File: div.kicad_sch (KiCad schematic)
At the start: 6 parts, among them X1 DF40HC_3.0_-100DS-0.4V_58, X2 DF40HC_3.0_-100DS-0.4V_58

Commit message: partnumber, manufaturerer and description cleanup completed
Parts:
- MP1, MP2, MP3, MP4: Description_1 steel, tin plated with internal thread M2.5 non stop outer 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 -> (none); MF Wurth Electronics -> (none); MP 9774030151R -> (none); MPN (none) -> 9774030151R; Manufacturer (none) -> Wurth Electronics
- X1, X2: Description_1 100 Position Connector Receptacle, Center Strip Contacts Su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 -> (none); MANUFACTURER HRS -> (none); MP DF40HC(3.0)-100DS-0.4V(58 -> (none); MPN (none) -> DF40HC(3.0)-100DS-0.4V(58; Manufacturer (none) -> HRS

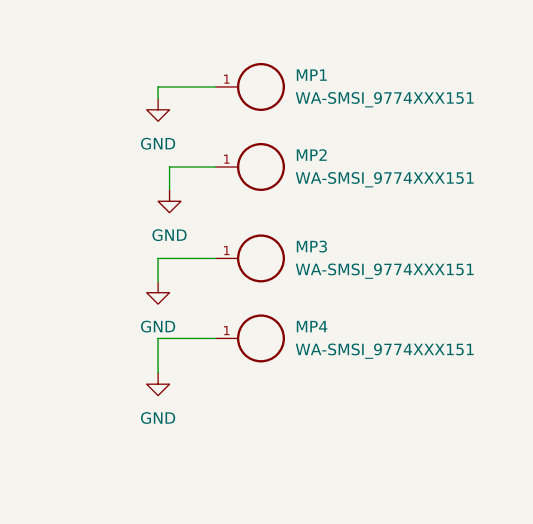
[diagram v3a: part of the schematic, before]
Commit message: update licence to CERN-OHL-S
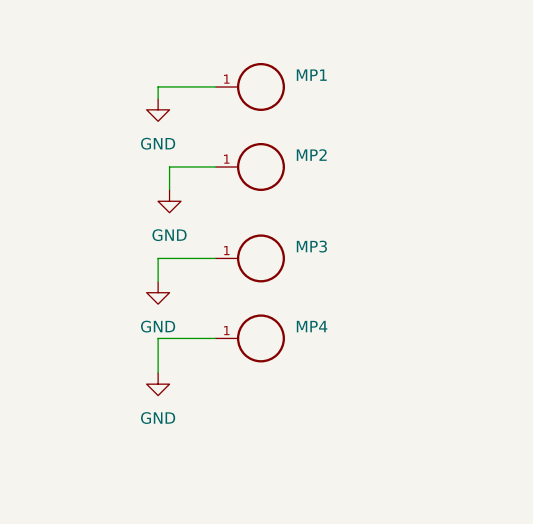
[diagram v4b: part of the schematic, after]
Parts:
- MP1, MP2, MP3, MP4: value WA-SMSI_9774XXX151 -> M2.5 x 3mm; VALUE M2.5 x 3mm -> (none)
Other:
- company: (none) -> NTNU, NINA
- title: (none) -> Audiograb
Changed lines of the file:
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@@
 (kicad_sch
-	(version 20250114)
+	(version 20260306)
 	(generator "eeschema")
-	(generator_version "9.0")
+	(generator_version "10.0")
 	(paper "A4")
+	(title_block
+		(title "Audiograb")
+		(date "2026-02-13")
+		(rev "0")
+		(company "NTNU, NINA")
+		(comment 1 "https://github.com/oveljosland/audiograb-pcb/")
+		(comment 2 "Licenced under CERN-OHL-S")
+	)

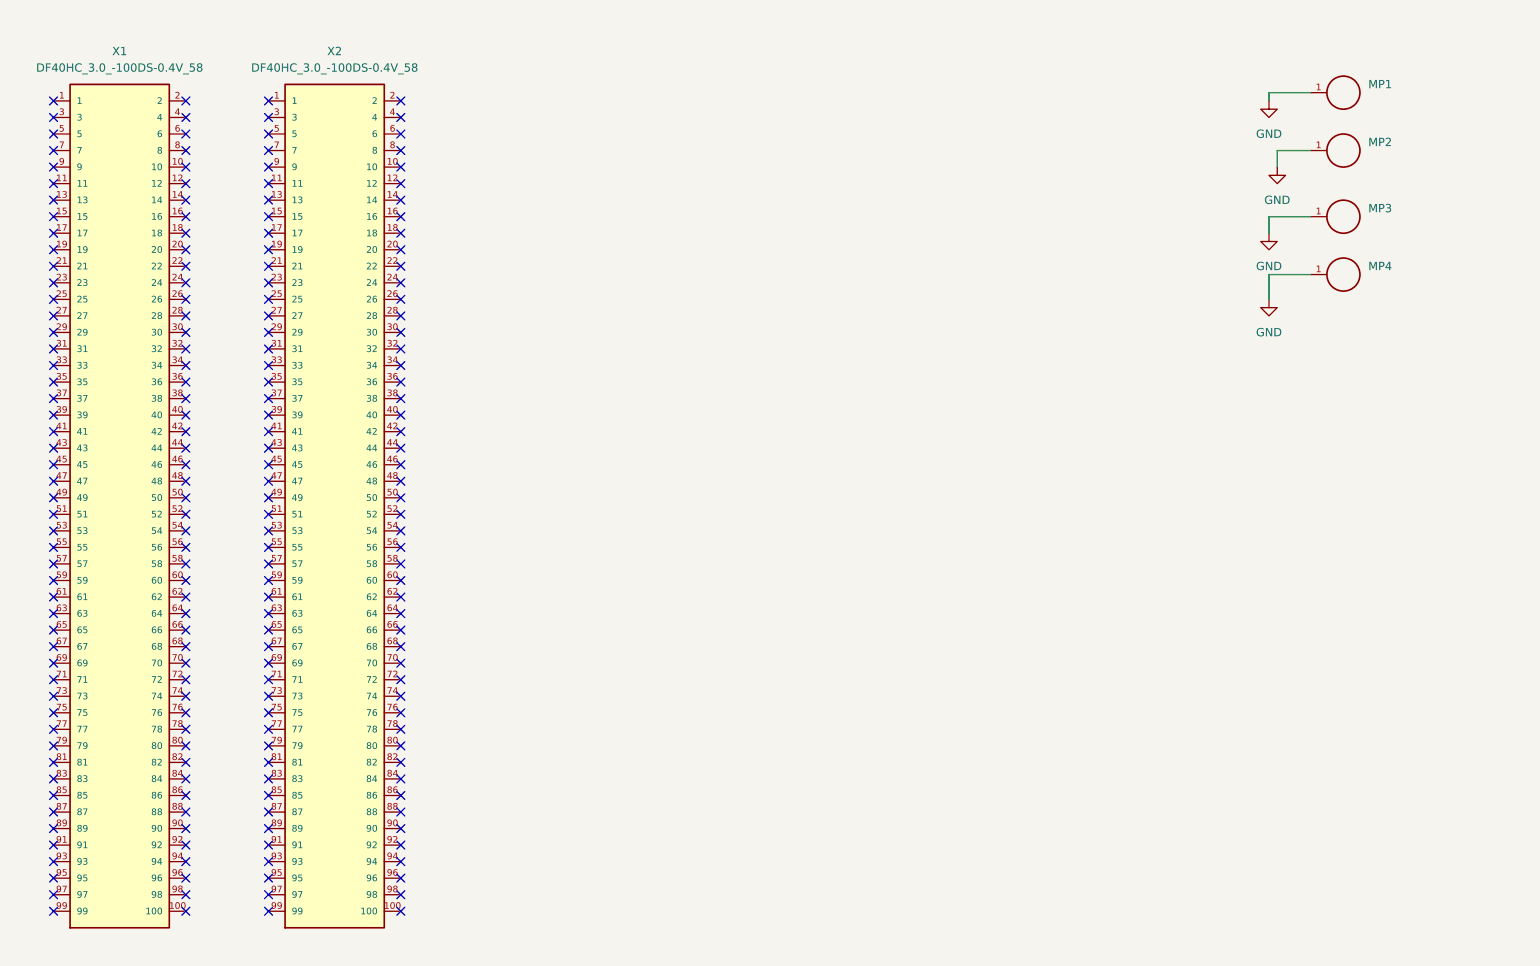
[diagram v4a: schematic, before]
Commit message: Ryddet i schematic og satt inn 3D figurer
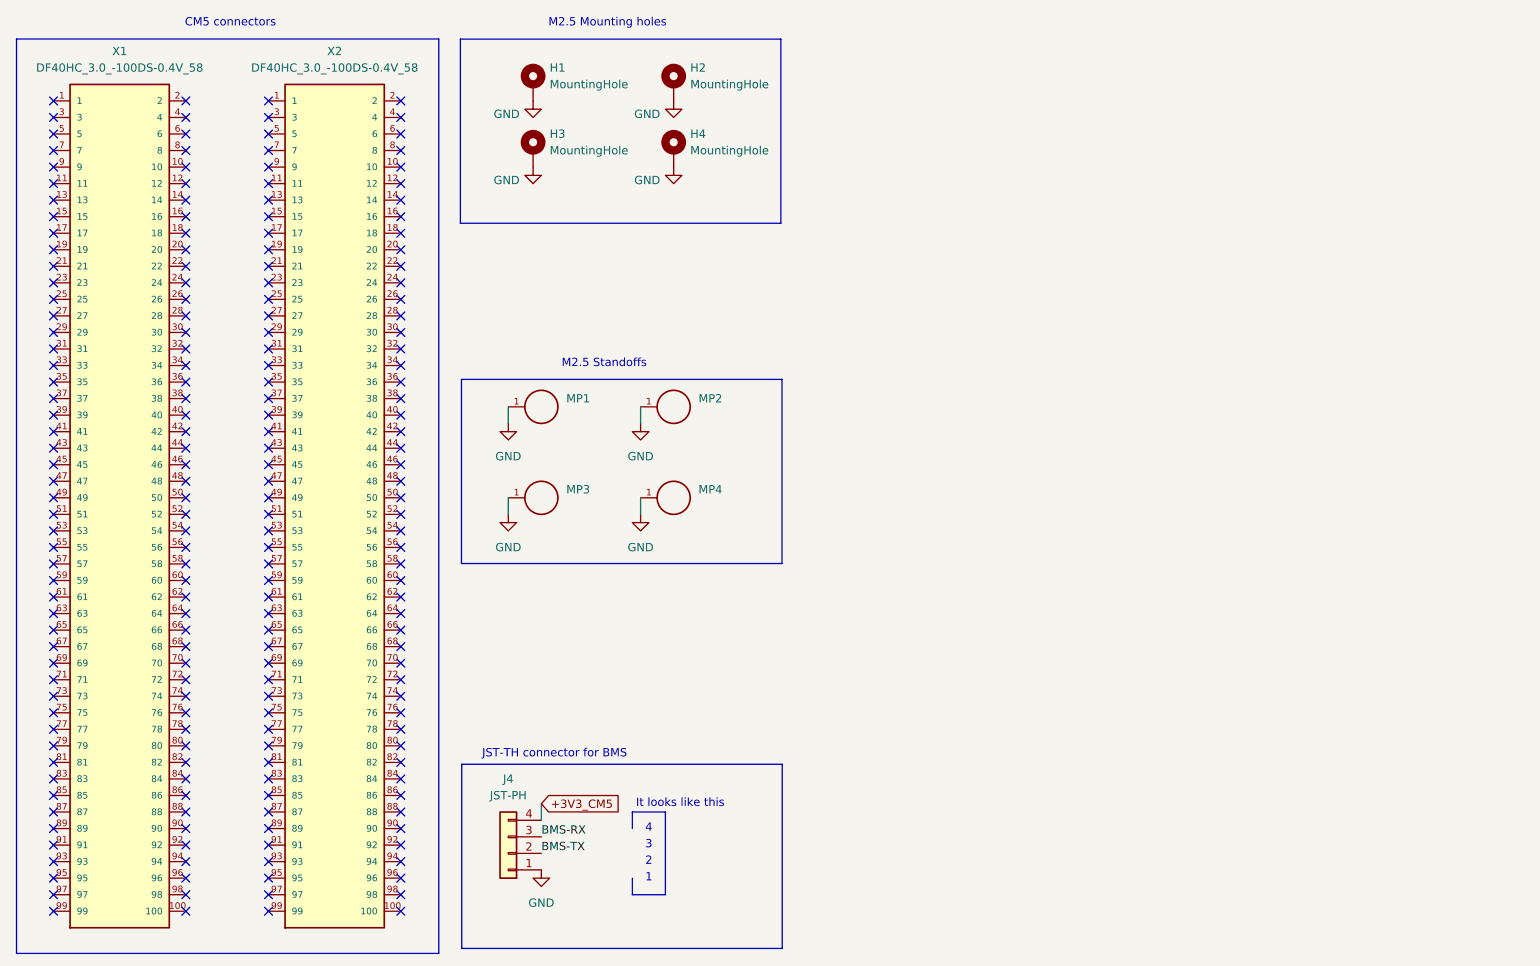
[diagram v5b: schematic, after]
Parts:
- added H1, H2, H3, H4: MountingHole, MountingHole:MountingHole_2.7mm_M2.5_ISO14580_Pad, symbol Mechanical:MountingHole_Pad
- added J4: JST-PH, Connector_JST:JST_PH_S4B-PH-K_1x04_P2.00mm_Horizontal, symbol PCM_4ms_Connector:Conn_01x04
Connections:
- net GND: now also H1.1, H2.1, H3.1, H4.1, J4.1 (Pin_1)
- new net +3V3_CM5: J4.4 (Pin_4)
- new net BMS-RX: J4.3 (Pin_3)
- new net BMS-TX: J4.2 (Pin_2)
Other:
- note added: "1"
- note added: "2"
- note added: "3"
- note added: "4"
- note added: "CM5 connectors"
- note added: "It looks like this"
- note added: "JST-TH connector for BMS"
- note added: "M2.5 Mounting holes"
- note added: "M2.5 Standoffs"
- moved on the sheet: MP1, MP2, MP3, MP4
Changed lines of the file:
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@@
 	(title_block
 		(title "Audiograb")
-		(date "2026-02-13")
-		(rev "0")
+		(date "2026-25-03")
+		(rev "1")
 		(company "NTNU, NINA")
 		(comment 1 "https://github.com/oveljosland/audiograb-pcb/")
